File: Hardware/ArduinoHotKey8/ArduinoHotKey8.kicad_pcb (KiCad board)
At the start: 2 copper layers, 96.5 x 77.5 mm, 39 parts, among them J1 AVR-ISP-6, SW0 SW_Push, SW1 SW_Push, SW2 SW_Push, SW3 SW_Push, SW4 SW_Push, SW5 SW_Push, SW6 SW_Push, SW7 SW_Push

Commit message: Minor improvement for USB connector
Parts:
- moved C3 5.12 mm to (75.0, 41.9)
- moved B1 1.27 mm to (77.5, 31.8)
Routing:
- net VCC: track 293.1 -> 300.6 mm
- net /BUTTON3: track 26.2 -> 24.7 mm
- net /BUTTON1: track 36.9 -> 35.7 mm
- net /BUTTON2: track 10.5 -> 9.25 mm
- net /RST: track 41.7 -> 42.4 mm
- net /MOSI: track 25.0 -> 24.4 mm
- net /BUTTON7: track 25.4 -> 25.9 mm
- net /BUTTON4: track 28.6 -> 28.0 mm
- net /BUTTON0: track 20.6 -> 20.1 mm
- net /BUTTON6: track 51.7 -> 52.2 mm

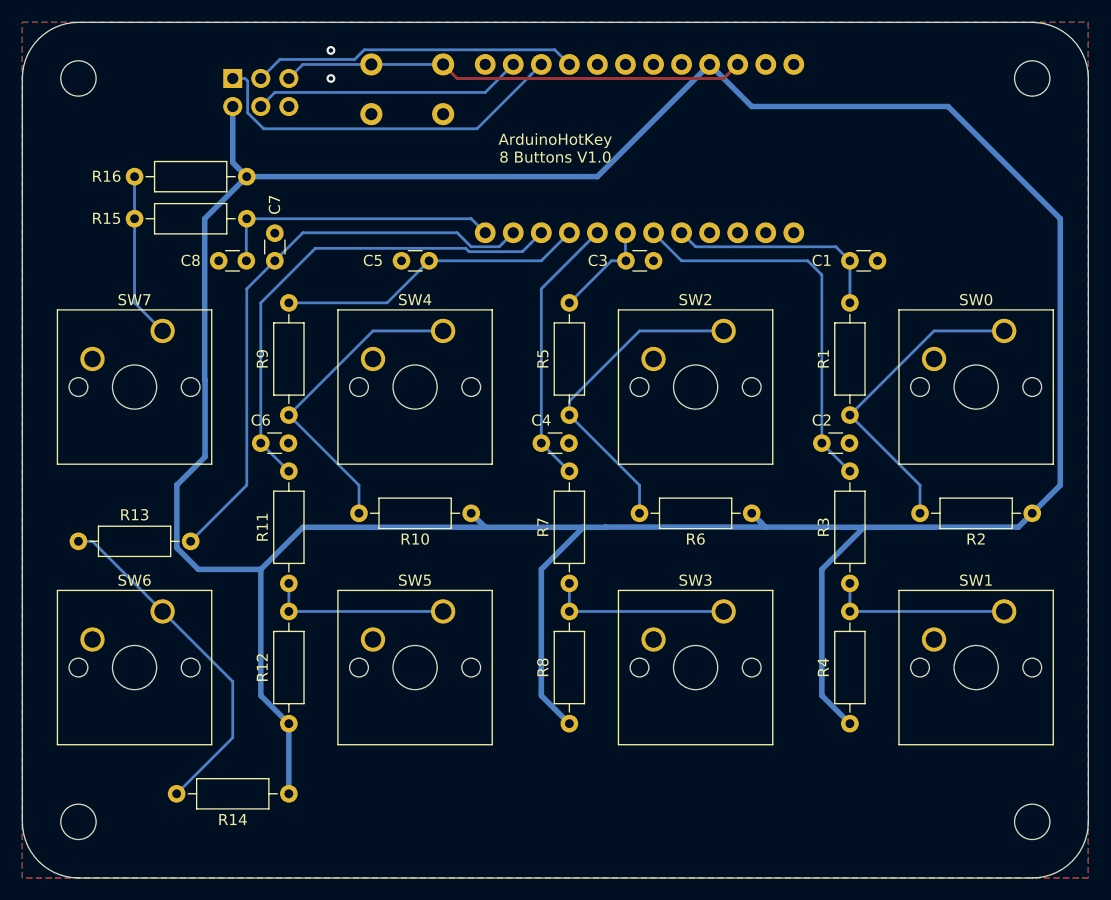
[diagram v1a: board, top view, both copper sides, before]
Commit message: Layout optimizations for USB Port
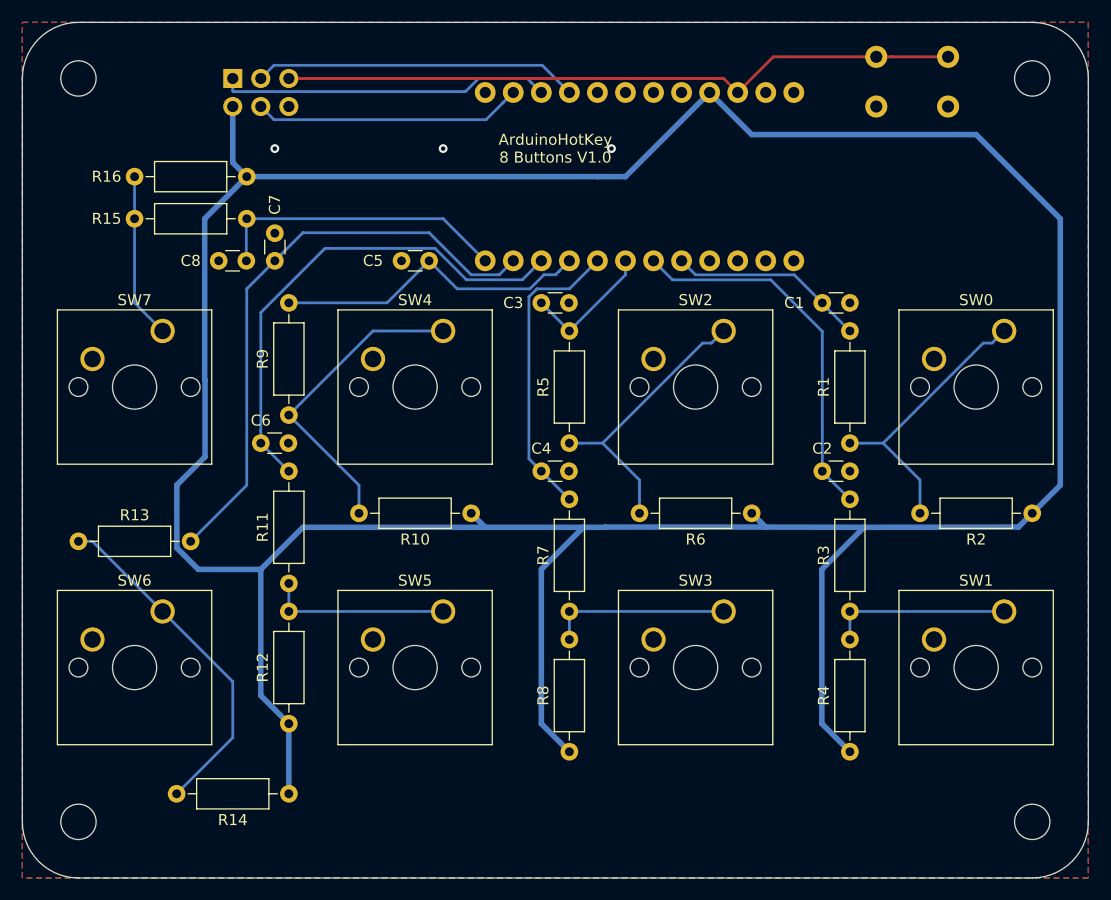
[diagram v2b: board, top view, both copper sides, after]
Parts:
- moved SW_Reset1 45.7 mm to (104.1, 23.4)
- moved C3 8.56 mm to (67.3, 45.7)
- moved C1 4.56 mm to (92.8, 45.7)
- moved C2 2.54 mm to (92.8, 61.0)
- moved R4 2.54 mm to (95.2, 86.4)
- moved R8 2.54 mm to (69.8, 86.4)
- moved B1 2.54 mm to (77.5, 34.3)
- moved C4 2.54 mm to (67.3, 61.0)
- moved R1 2.54 mm to (95.2, 58.4)
- moved R5 2.54 mm to (69.8, 58.4)
- moved R3 2.54 mm to (95.2, 73.7)
- moved R7 2.54 mm to (69.8, 73.7)
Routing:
- net /RST: track 42.4 -> 61.6 mm
- net /MISO: track 33.9 -> 30.1 mm
- net Net-(R5-Pad1): track 29.4 -> 25.9 mm
- net VCC: track 300.6 -> 303.6 mm
- net /BUTTON2: track 9.25 -> 12.0 mm
- net Net-(R1-Pad1): track 28.6 -> 25.9 mm
- net /BUTTON3: track 24.7 -> 27.4 mm
- net /BUTTON0: track 20.1 -> 17.9 mm
- net /BUTTON1: track 35.7 -> 34.2 mm
- net /BUTTON4: track 28.0 -> 29.1 mm
- net /BUTTON7: track 25.9 -> 27.0 mm
- net /BUTTON6: track 52.2 -> 53.3 mm
- net /BUTTON5: track 44.6 -> 45.1 mm
- net GND: vias 2 -> 3
